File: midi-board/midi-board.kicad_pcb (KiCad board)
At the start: 2 copper layers, 88 x 45 mm, 39 parts, among them J1 MIDI OUT, J2 MIDI IN, J3 Qwiic, J4 A0, J5 A1, J6 Qwiic, J7 UART, U1 74LVC1G06, U2 74LVC1G17, U3 TLP185(SE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

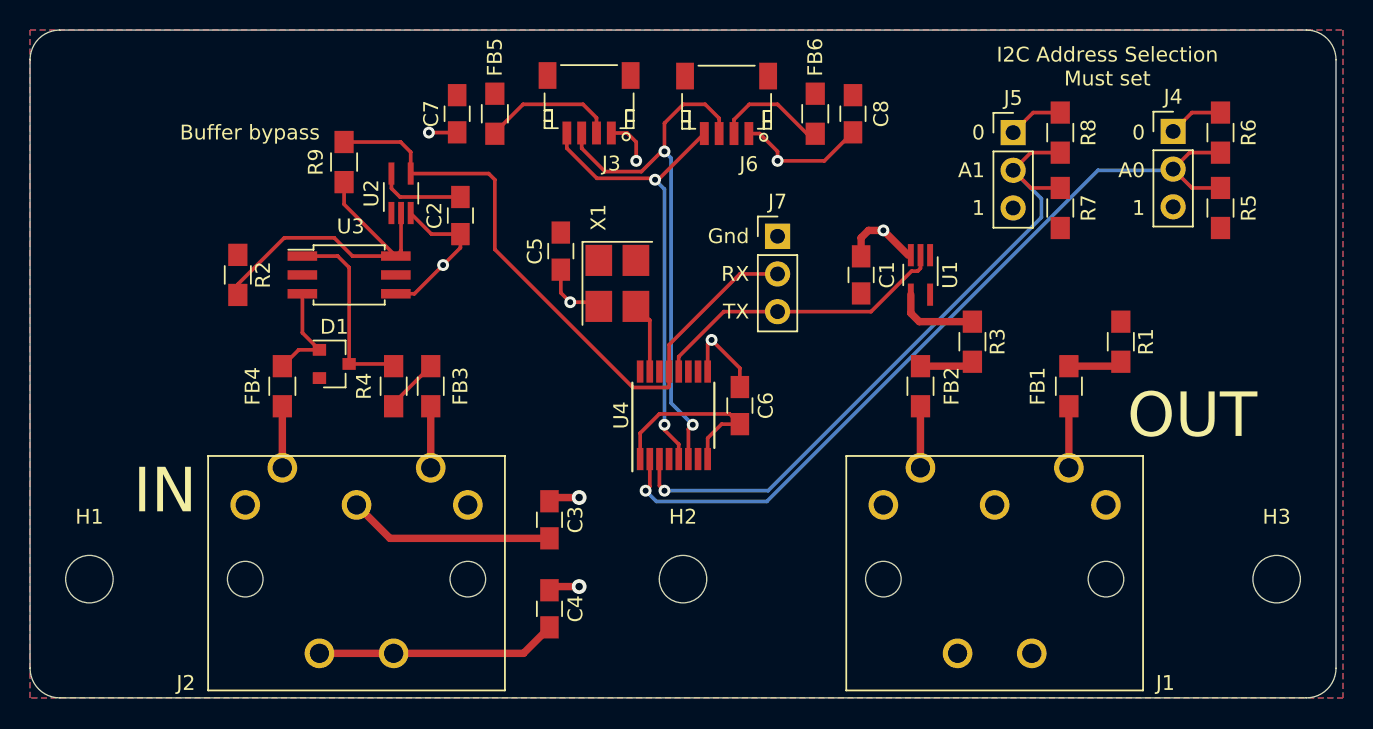
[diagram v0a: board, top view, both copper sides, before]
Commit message: Remove unnecessary buffer, finish up reset line(s).
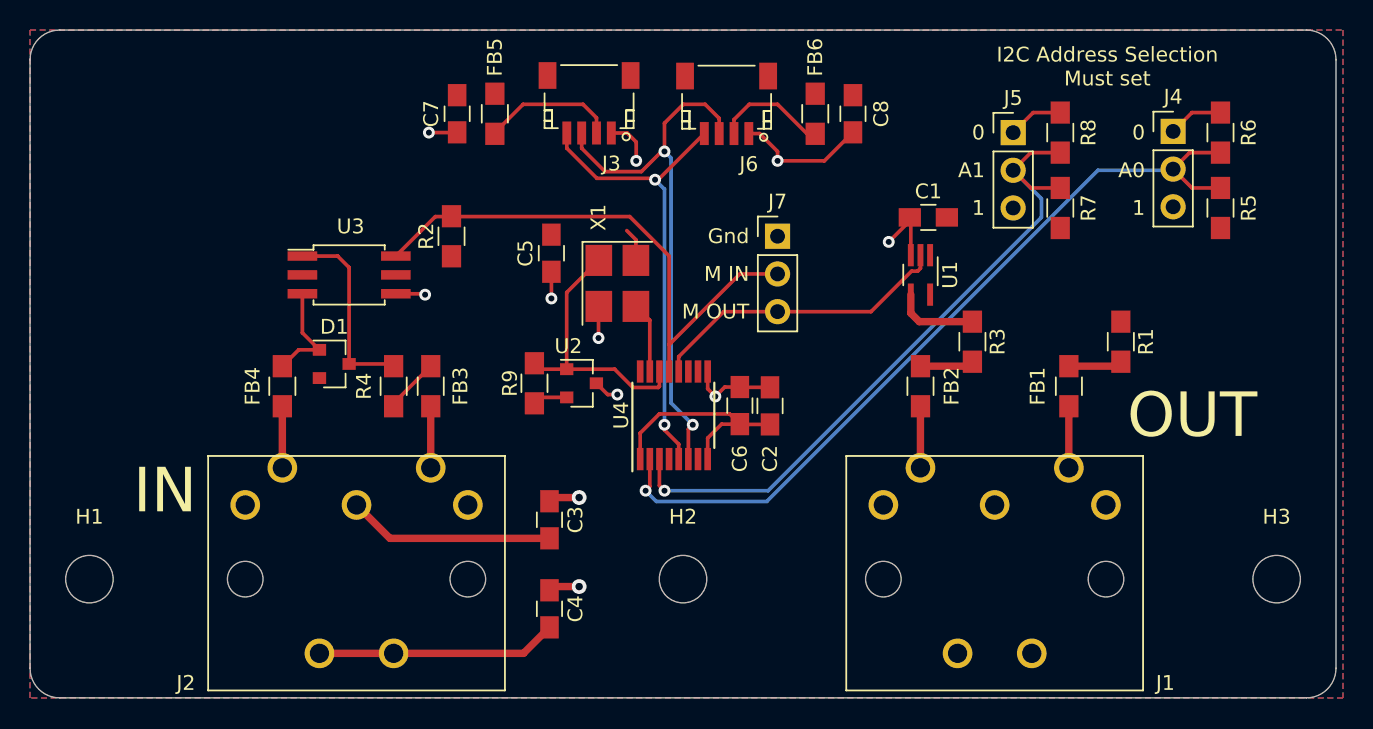
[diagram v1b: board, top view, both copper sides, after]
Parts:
- C2: value 0.1uF -> 4.7uF
- R9: value DNP -> 0/DNP
- U2: value 74LVC1G17 -> MCP1X0-315; footprint TO_SOT_Packages_SMD:SOT-353_SC-70-5_Handsoldering -> TO_SOT_Packages_SMD:SOT-23
- moved C2 24.5 mm to (165.9, 60.3), turned to 270 degrees
- moved R9 19.7 mm to (150.0, 58.8)
- moved U2 17.7 mm to (153.2, 58.8), turned to 0 degrees
- moved R2 14.6 mm to (144.4, 48.9), turned to 90 degrees
- moved C1 5.96 mm to (176.5, 47.6), turned to 0 degrees
- moved C5 0.65 mm to (151.1, 50.0)
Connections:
- R2 pad 2: Net-(R2-Pad2) -> /RX
- R9 pad 1: /RX -> Net-(R9-Pad1)
- R9 pad 2: Net-(R2-Pad2) -> +3V3
- U2 pad 1: (no net) -> Net-(R9-Pad1)
- U2 pad 2: Net-(R2-Pad2) -> +3V3
- U3 pad 6: Net-(R2-Pad2) -> /RX
- U4 pad 14: (no net) -> Net-(R9-Pad1)
- X1 pad 1: +3V3 -> Net-(R9-Pad1)
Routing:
- net Net-(R2-Pad2): track 22.6 -> 0.00 mm
- net Net-(R9-Pad1): track 0.00 -> 18.4 mm
- net GND: track 52.4 -> 44.4 mm, vias 9 -> 11
- net /RX: track 44.5 -> 37.7 mm
- net +3V3: track 19.2 -> 19.9 mm
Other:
- board text added: "M IN"
- board text added: "M OUT"
- board text removed: "Buffer bypass"
- board text removed: "RX"
- board text removed: "TX"

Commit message: MIDI board Rev 1 changes
* Standardize mounting hole spacing
* Change 74LVC1G06 to 74LVC1G07 in schematic
* Expose ~IRQ headers
* Increase Qwiic header space
* Improve TLP185(SE footprint; remove unused pads, label orientation
* Bring I2C out on a header.
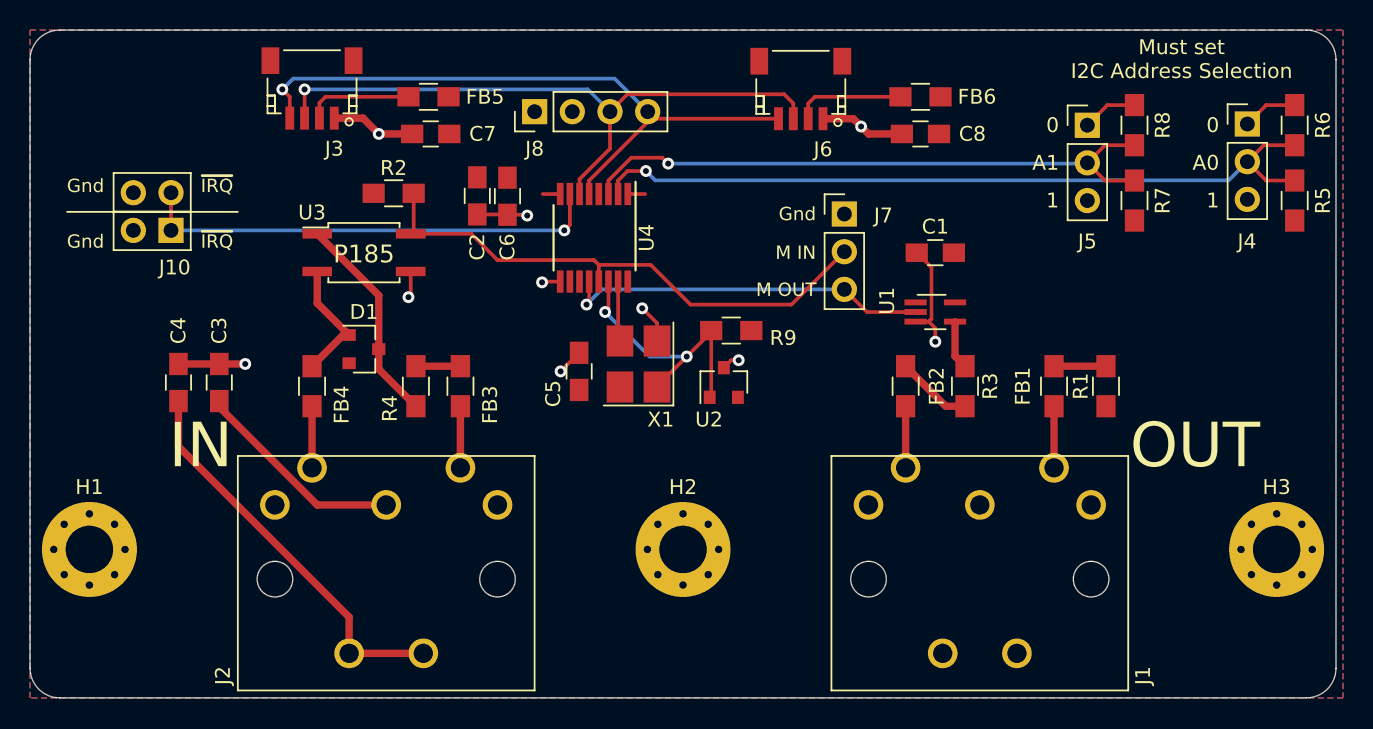
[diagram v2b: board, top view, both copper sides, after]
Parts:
- added J10: Conn_02x02_Odd_Even, Pin_Headers:Pin_Header_Straight_2x02_Pitch2.54mm, F.Cu at (125.5, 48.5)
- added J8: I2C, Pin_Headers:Pin_Header_Straight_1x04_Pitch2.54mm, F.Cu at (150.0, 40.5)
- H1, H2, H3: footprint Mounting_Holes:MountingHole_3.2mm_M3 -> Mounting_Holes:MountingHole_3.2mm_M3_Pad_Via
- U1: value 74LVC1G06 -> 74LVC1G07
- moved C4 29.3 mm to (126.0, 58.8)
- moved C2 24.3 mm to (146.1, 46.2), turned to 90 degrees
- moved C3 24.1 mm to (128.8, 58.8)
- moved C6 21.1 mm to (148.2, 46.2), turned to 90 degrees
- moved J3 18.7 mm to (135.0, 39.0)
- moved R9 13.7 mm to (163.2, 55.2), turned to 0 degrees
- moved U4 13.1 mm to (154.0, 49.0), turned to 270 degrees
- moved U2 9.59 mm to (162.8, 58.8), turned to 90 degrees
- moved C5 8.18 mm to (153.0, 58.0), turned to 270 degrees
- moved FB6 7.18 mm to (176.0, 39.5), turned to 0 degrees
- moved X1 5.61 mm to (157.0, 57.5), turned to 90 degrees
- moved J6 5.10 mm to (167.9, 39.0)
- moved J4 5.02 mm to (198.0, 41.3)
- moved J5 5.02 mm to (187.2, 41.4)
- moved R5 5.02 mm to (201.2, 46.5)
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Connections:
- net Net-(R9-Pad1) renamed /~RST
- net Net-(U4-Pad15) renamed /CLK
- U4 pad 7: (no net) -> /~IRQ
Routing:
- net /~IRQ: track 0.00 -> 31.6 mm, vias 0 -> 1
- net +3V3: track 19.9 -> 2.40 mm
- net /SCL: track 31.9 -> 44.2 mm, vias 2 -> 1
- net Net-(C4-Pad2): track 16.2 -> 26.8 mm
- net /SDA: track 36.9 -> 43.7 mm, vias 2 -> 1
- net /A1: track 46.6 -> 41.3 mm
- net /TX: track 20.6 -> 25.0 mm, vias 0 -> 1
- net /A0: track 54.7 -> 51.7 mm
- net Net-(R3-Pad1): track 5.64 -> 3.28 mm
- net Net-(FB5-Pad1): track 9.12 -> 7.20 mm
- net Net-(FB2-Pad1): track 3.62 -> 5.12 mm
- net Net-(D1-Pad1): track 13.0 -> 14.4 mm
- net Net-(D1-Pad2): track 7.21 -> 8.54 mm
- net GND: track 44.4 -> 43.3 mm, vias 11 -> 10
- net /RX: track 37.7 -> 36.9 mm
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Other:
- board text added: "I2C↔MIDI Rev0 http://github.com/jkominek/piano-conversion"
- board text added: "Must set I2C Address Selection"
- board text added: "P185"
- board text added: "~IRQ"
- board text removed: "I2C Address Selection Must set"
- board text removed: "TTL↔MIDI Rev0 http://github.com/jkominek/piano-conversion"
